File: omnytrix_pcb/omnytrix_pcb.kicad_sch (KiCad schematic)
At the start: 15 parts, among them U1 LD3985M33R_SOT23, U3 STM32F411RCTx

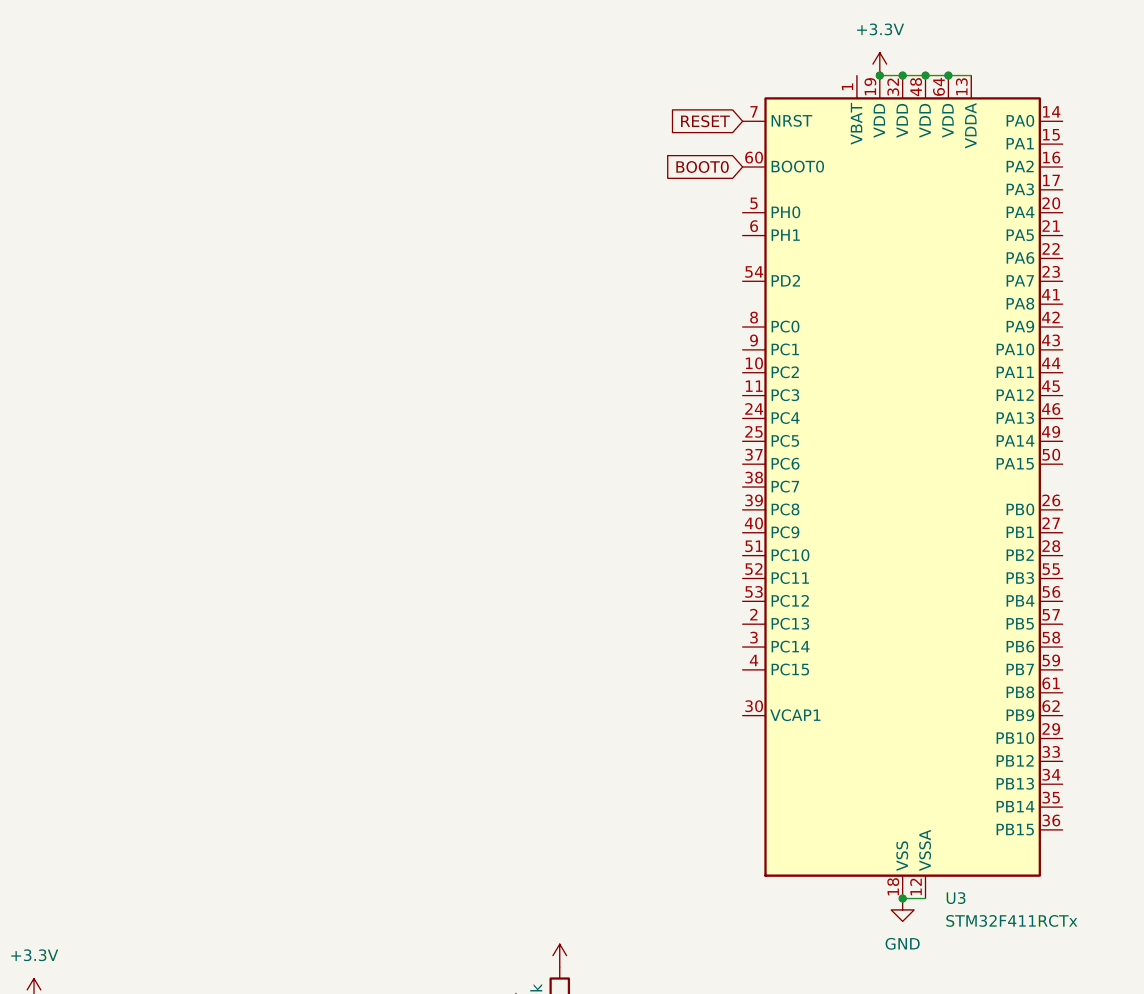
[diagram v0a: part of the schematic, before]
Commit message: add some R and change position of components
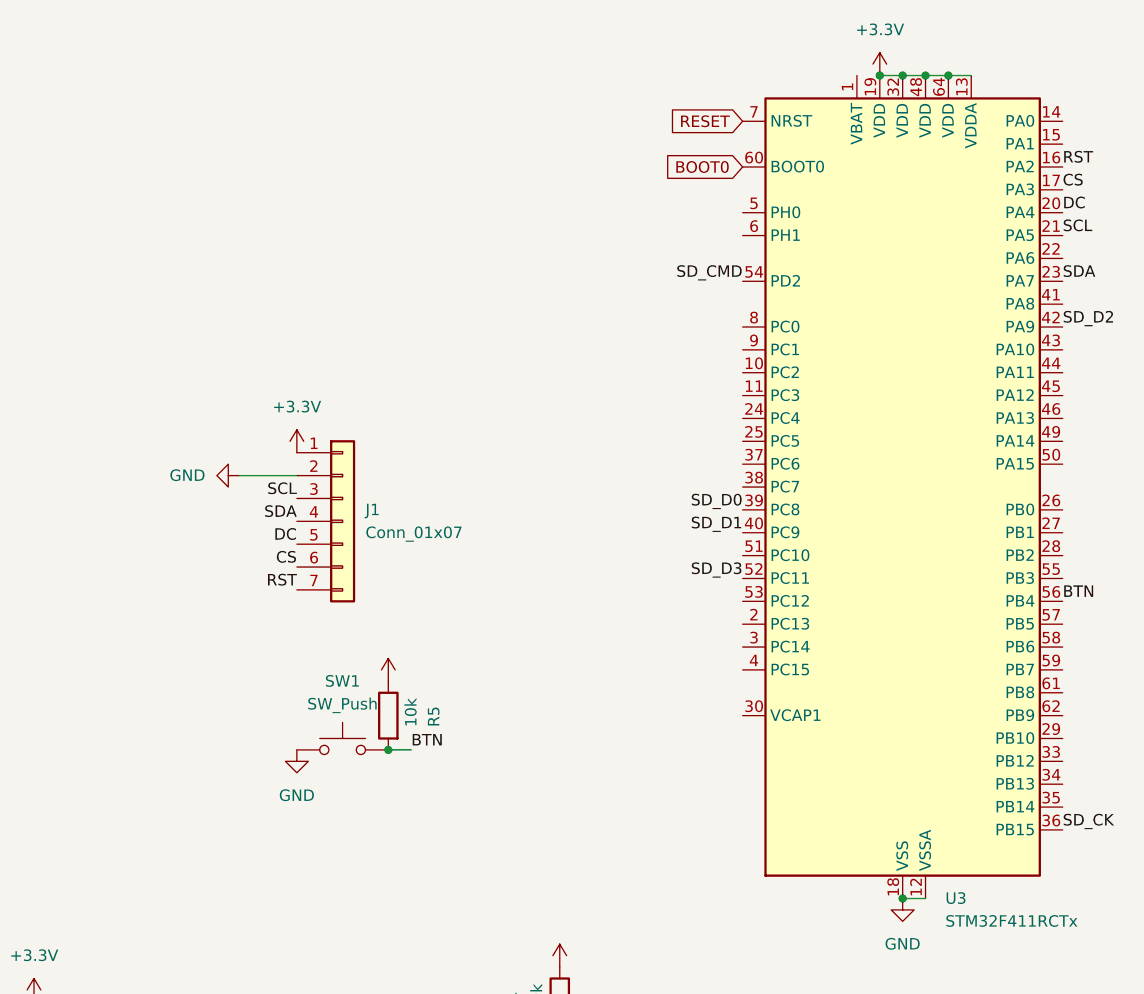
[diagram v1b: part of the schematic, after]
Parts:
- added J1: Conn_01x07, Connector_PinHeader_2.54mm:PinHeader_1x07_P2.54mm_Vertical, symbol Connector_Generic:Conn_01x07
- added R5: 10k, Resistor_SMD:R_0603_1608Metric_Pad0.98x0.95mm_HandSolder, symbol Device:R
- added SW1: SW_Push, Button_Switch_Keyboard:SW_Cherry_MX_1.00u_PCB, symbol Switch:SW_Push
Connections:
- net +3.3V: now also J1.1 (Pin_1), R5.1
- net GND: now also J1.2 (Pin_2), SW1.1
- net RST: now reaches U3.16 (PA2)
- net RST: now also J1.7 (Pin_7)
- net CS: now reaches U3.17 (PA3)
- net CS: now also J1.6 (Pin_6)
- net DC: now reaches U3.20 (PA4)
- net DC: now also J1.5 (Pin_5)
- net SCL: now reaches U3.21 (PA5)
- net SCL: now also J1.3 (Pin_3)
- net SDA: now reaches U3.23 (PA7)
- net SDA: now also J1.4 (Pin_4)
- net SD_CK: now reaches U3.36 (PB15)
- net SD_D0: now reaches U3.39 (PC8)
- net SD_D1: now reaches U3.40 (PC9)
- net SD_D2: now reaches U3.42 (PA9)
- net SD_D3: now reaches U3.52 (PC11)
- net SD_CMD: now reaches U3.54 (PD2)
- net BTN: now reaches U3.56 (PB4)
- net BTN: now also R5.2, SW1.2

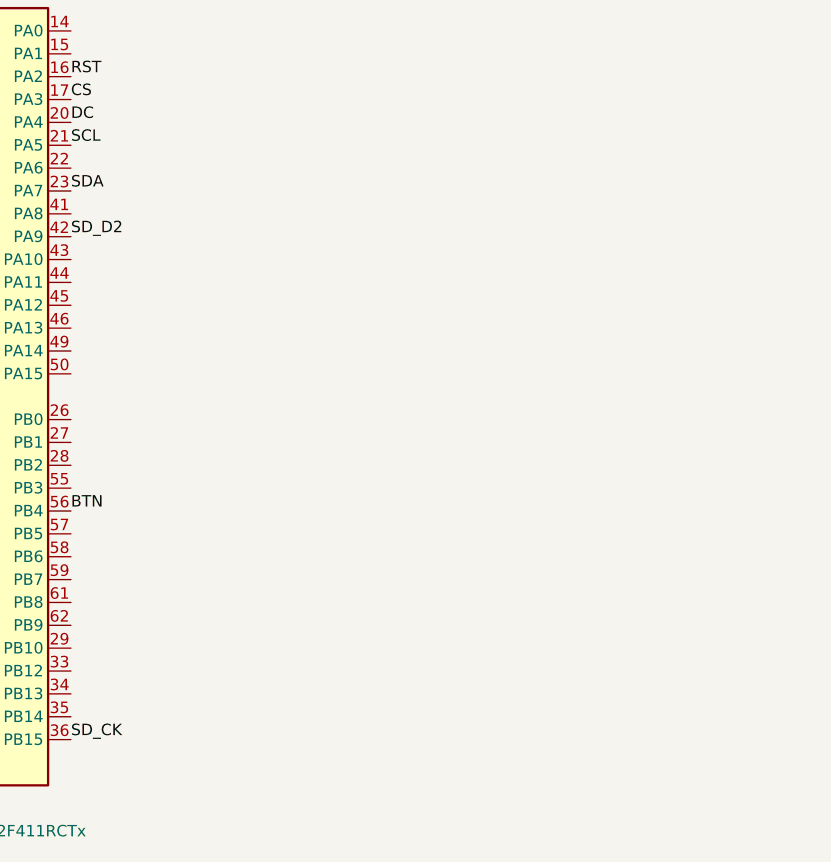
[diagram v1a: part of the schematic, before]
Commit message: add microsd
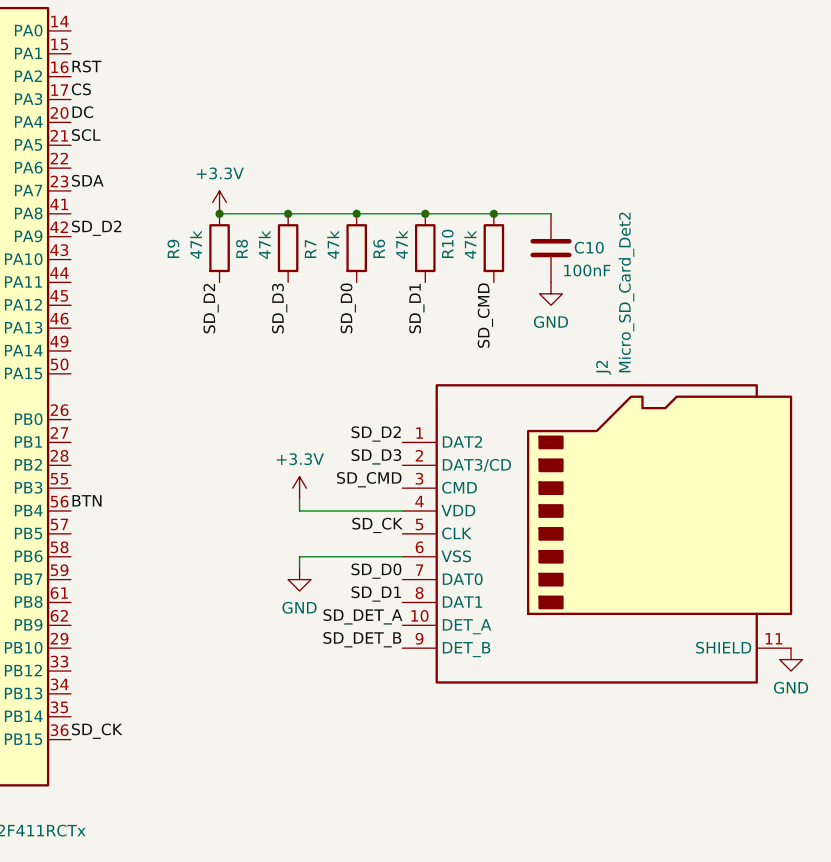
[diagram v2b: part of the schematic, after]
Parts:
- added C10: 100nF, Capacitor_SMD:C_0603_1608Metric_Pad1.08x0.95mm_HandSolder, symbol Device:C
- added J2: Micro_SD_Card_Det2, libs:microSD_molex, symbol Connector:Micro_SD_Card_Det2
- added R10, R6, R7, R8, R9: 47k, Resistor_SMD:R_0603_1608Metric_Pad0.98x0.95mm_HandSolder, symbol Device:R
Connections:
- net +3.3V: now also C10.1, J2.4 (VDD), R10.1, R6.1, R7.1, R8.1, R9.1
- net GND: now also C10.2, J2.11 (SHIELD), J2.6 (VSS)
- net SD_CK: now also J2.5 (CLK)
- net SD_CMD: now also J2.3 (CMD), R10.2
- net SD_D0: now also J2.7 (DAT0), R7.2
- net SD_D1: now also J2.8 (DAT1), R6.2
- net SD_D2: now also J2.1 (DAT2), R9.2
- net SD_D3: now also J2.2 (DAT3/CD), R8.2
- new net SD_DET_A: J2.10 (DET_A)
- new net SD_DET_B: J2.9 (DET_B)

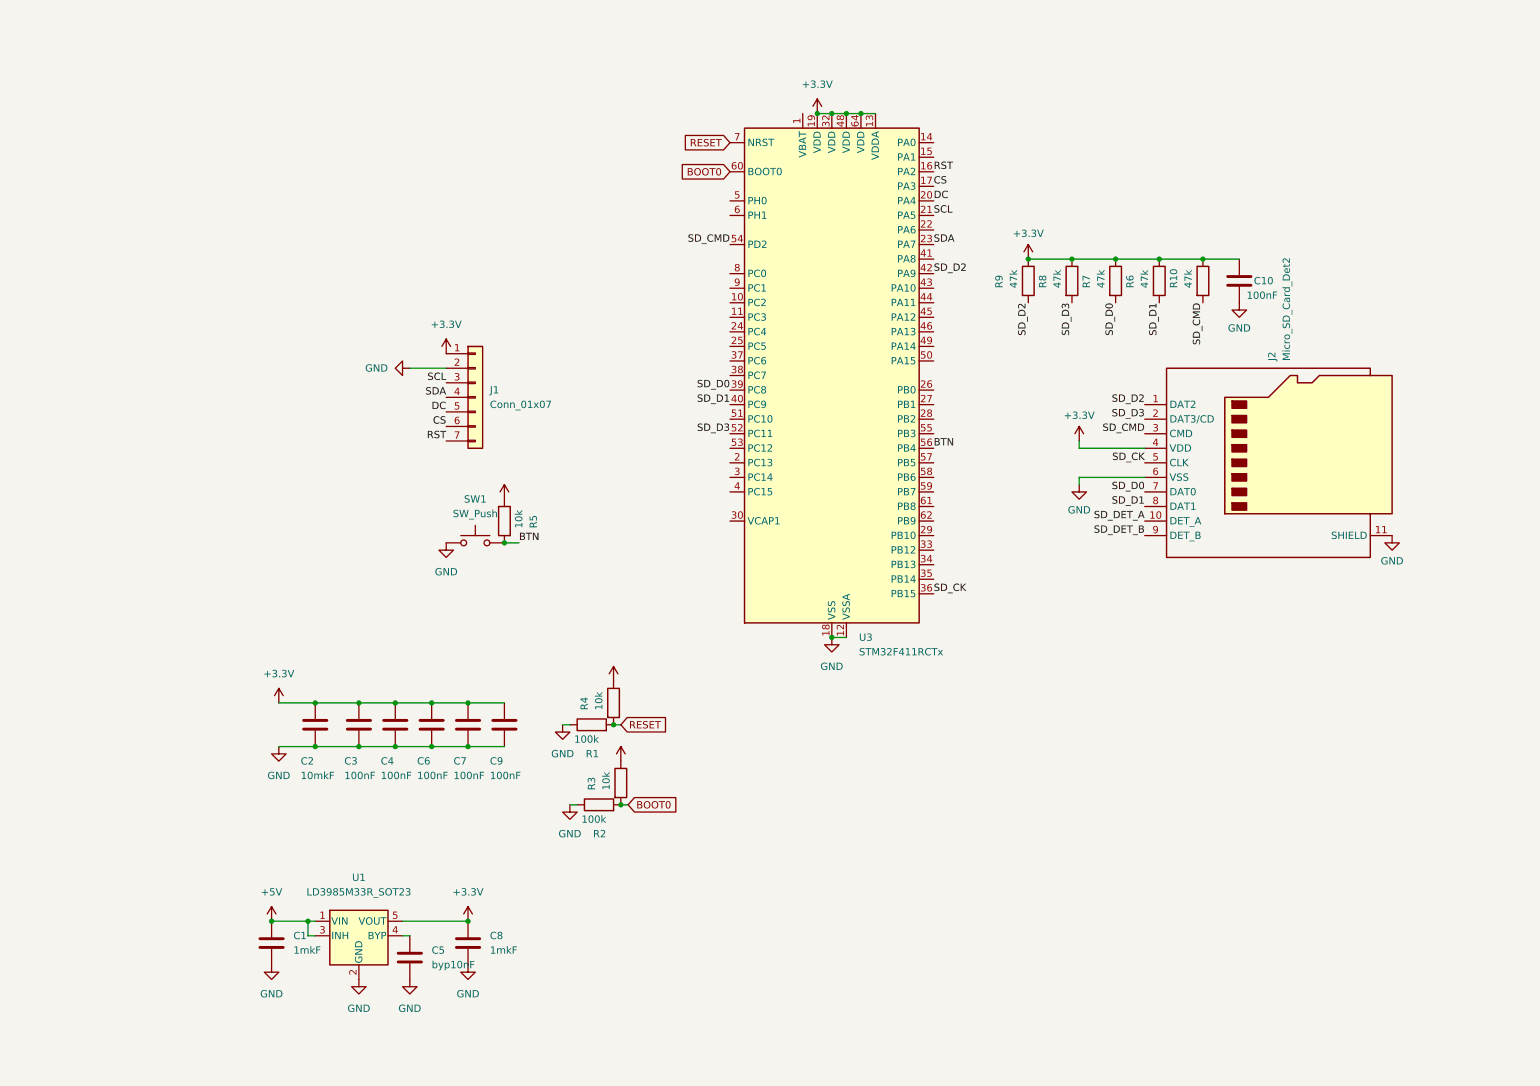
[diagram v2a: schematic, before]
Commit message: add bat control
Add battery controller TP4056
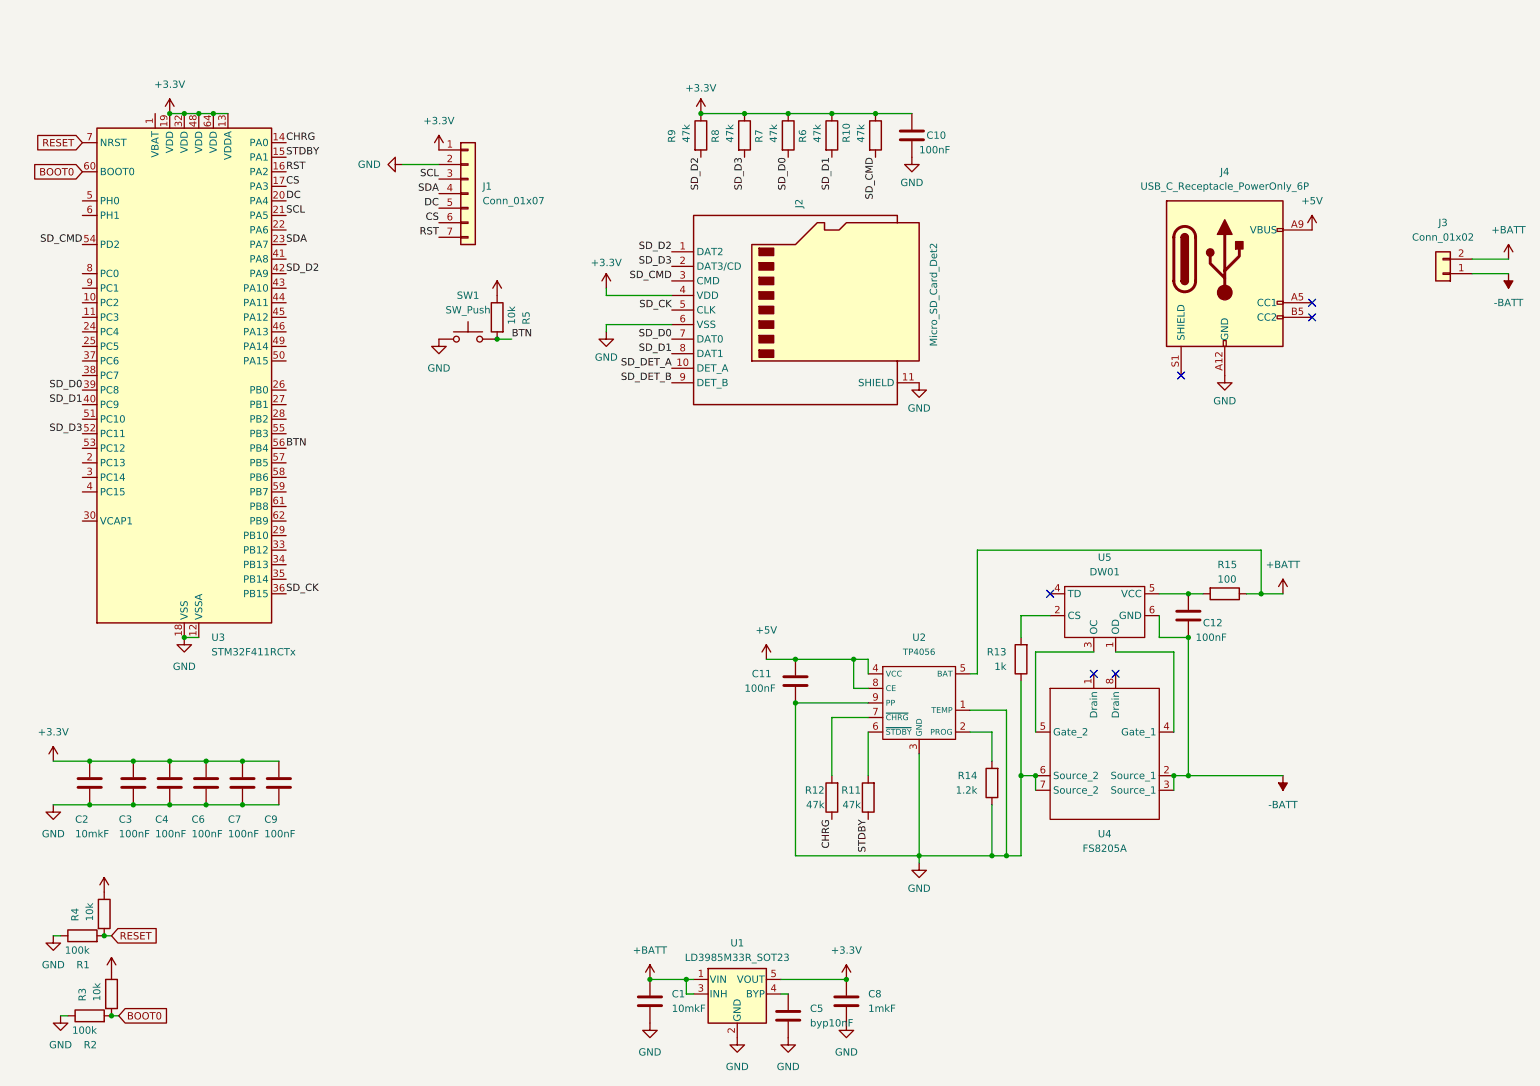
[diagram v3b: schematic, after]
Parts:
- added C11, C12: 100nF, Capacitor_SMD:C_0603_1608Metric_Pad1.08x0.95mm_HandSolder, symbol Device:C
- added J3: Conn_01x02, Connector_PinHeader_2.00mm:PinHeader_1x02_P2.00mm_Vertical, symbol Connector_Generic:Conn_01x02
- added J4: USB_C_Receptacle_PowerOnly_6P, Connector_USB:USB_C_Receptacle_HRO_TYPE-C-31-M-12, symbol Connector:USB_C_Receptacle_PowerOnly_6P
- added R11, R12: 47k, Resistor_SMD:R_0603_1608Metric_Pad0.98x0.95mm_HandSolder, symbol Device:R
- added R13: 1k, Resistor_SMD:R_0603_1608Metric_Pad0.98x0.95mm_HandSolder, symbol Device:R
- added R14: 1.2k, Resistor_SMD:R_0603_1608Metric_Pad0.98x0.95mm_HandSolder, symbol Device:R
- added R15: 100, Resistor_SMD:R_0603_1608Metric_Pad0.98x0.95mm_HandSolder, symbol Device:R
- added U2: TP4056, Package_SO:SOIC-8-1EP_3.9x4.9mm_P1.27mm_EP2.29x3mm, symbol libs:TP4056
- added U4: FS8205A, Package_SO:TSSOP-8_4.4x3mm_P0.65mm, symbol libs:FS8205A
- added U5: DW01, Package_TO_SOT_SMD:SOT-23-6_Handsoldering, symbol libs:DW01
- C1: value 1mkF -> 10mkF
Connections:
- net +5V: now also C11.1, J4.A9 (VBUS), J4.B9 (VBUS), U2.4 (VCC), U2.8 (CE); no longer C1.1, U1.1 (VIN), U1.3 (INH)
- net GND: now also C11.2, J4.A12 (GND), J4.B12 (GND), R13.1, R14.1, U2.1 (TEMP), U2.3 (GND), U2.9 (PP), U4.6 (Source_2), U4.7 (Source_2)
- net CHRG: now reaches U3.14 (PA0)
- net CHRG: now also R12.1
- net STDBY: now reaches U3.15 (PA1)
- net STDBY: now also R11.1
- new net: R14.2, U2.2 (PROG)
- new net: R11.2, U2.6 (~{STDBY})
- new net: R12.2, U2.7 (~{CHRG})
- new net: C12.1, R15.2, U5.5 (VCC)
- new net: U4.4 (Gate_1), U5.1 (OD)
- new net: R13.2, U5.2 (CS)
- new net: U4.5 (Gate_2), U5.3 (OC)
- new net +BATT: C1.1, J3.2 (Pin_2), R15.1, U1.1 (VIN), U1.3 (INH), U2.5 (BAT)
- new net -BATT: C12.2, J3.1 (Pin_1), U4.2 (Source_1), U4.3 (Source_1), U5.6 (GND)
- no-connect marks 0 -> 6
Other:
- moved on the sheet: C1, C10, C2, C3, C4, C5, C6, C7, C8, C9, J1, J2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
